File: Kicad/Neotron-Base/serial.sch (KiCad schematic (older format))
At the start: 7 parts, among them J601 Conn_02x05, U601 ICL3232CPZMAX

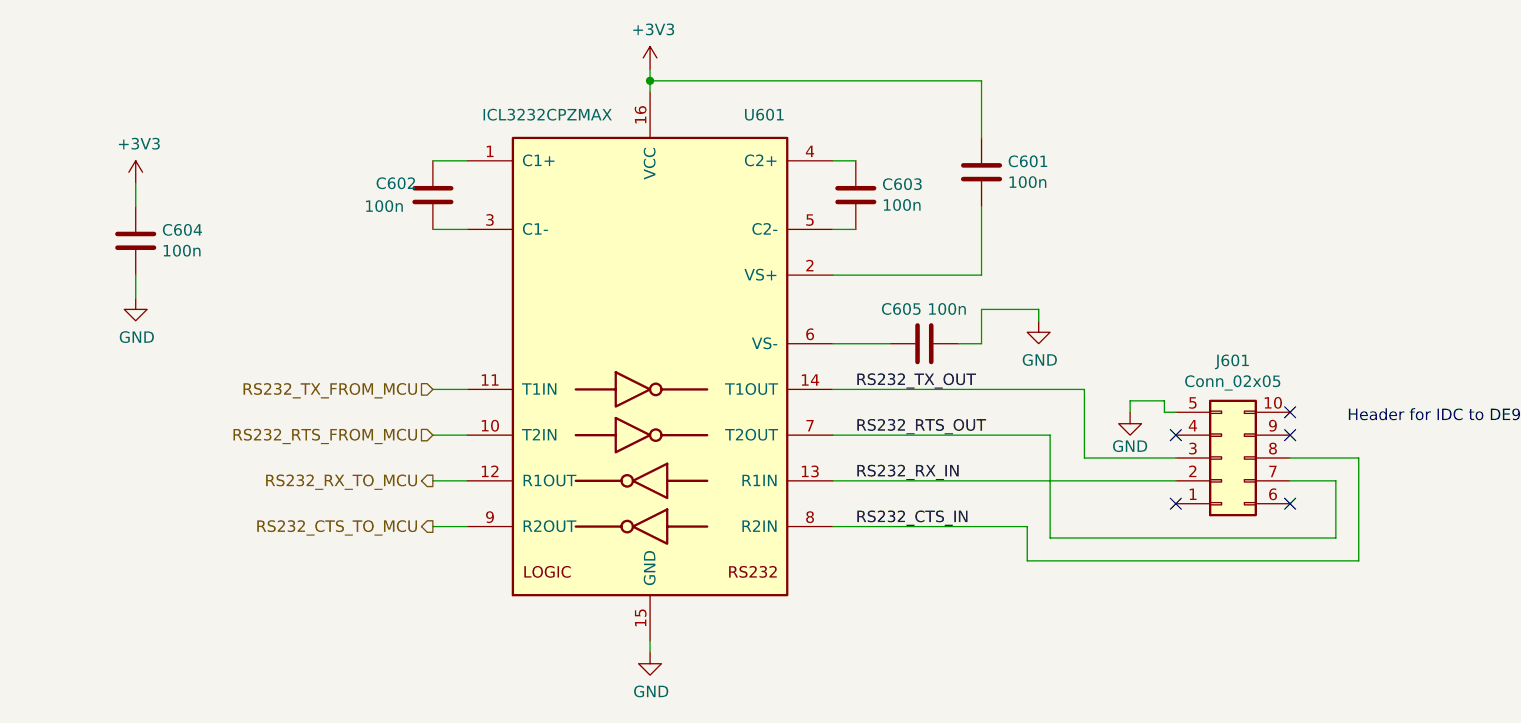
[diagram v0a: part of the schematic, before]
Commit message: Re-work CPU interface to include RMII.
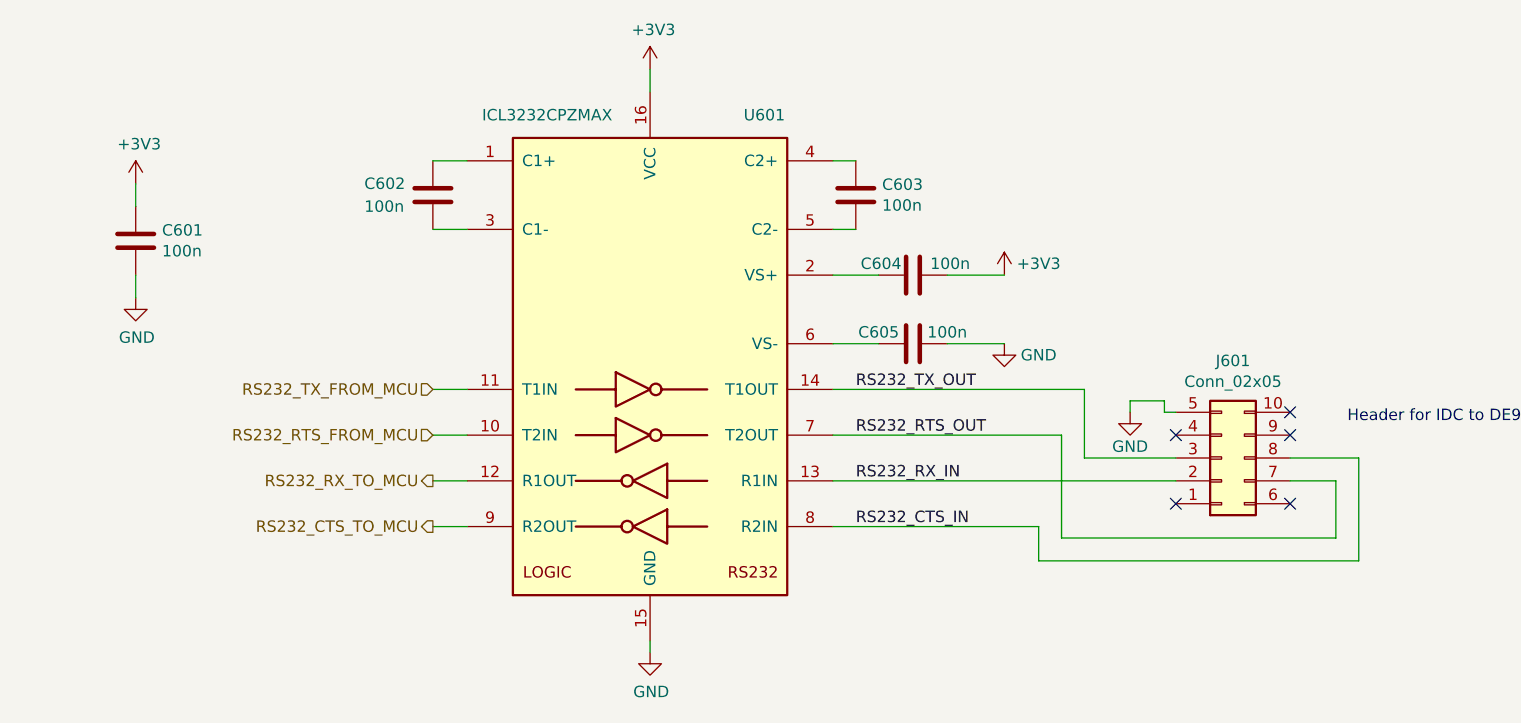
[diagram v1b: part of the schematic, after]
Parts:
- renumbered C604 to C601, C601 to C604
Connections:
- net +3V3: now also C604.2; no longer C604.1
- net at U601.2 (VS+): now also C604.1; no longer C604.2
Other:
- moved on the sheet: C604, C605
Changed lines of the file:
@@
 $Descr A4 11693 8268
 encoding utf-8
-Sheet 6 7
+Sheet 6 10
 Title "Neotron Base - RS-232 Interface"
-Date "2020-08-07"
+Date "2020-08-15"
 Rev "[Uncontrolled]"
 Comp "github.com/neotron-compute"
@@
 L power:GND #PWR?
 U 1 1 5E180507
-P 7300 3450
-F 0 "#PWR?" H 7300 3200 50  0001 C CNN
-F 1 "GND" H 7305 3277 50  0000 C CNN
-F 2 "" H 7300 3450 50  0001 C CNN
-F 3 "" H 7300 3450 50  0001 C CNN
-	1    7300 3450
-	1    0    0    -1
-$EndComp
-Wire Wire Line
-	7300 3450 7300 3400
+P 7150 3550
+F 0 "#PWR?" H 7150 3300 50  0001 C CNN
+F 1 "GND" H 7300 3500 50  0000 C CNN
+F 2 "" H 7150 3550 50  0001 C CNN
+F 3 "" H 7150 3550 50  0001 C CNN
+	1    7150 3550
+	1    0    0    -1
+$EndComp
 $Comp
 L Device:C C603
@@
 L Device:C C605
 U 1 1 5E182C3F
-P 6800 3550
-F 0 "C605" V 6650 3450 50  0000 C CNN
-F 1 "100n" V 6650 3650 50  0000 C CNN
-F 2 "Capacitor_THT:C_Disc_D3.0mm_W2.0mm_P2.50mm" H 6838 3400 50  0001 C CNN
-F 3 "~" H 6800 3550 50  0001 C CNN
-F 4 "Vishay" H 0   0   50  0001 C CNN "Manufacturer"
-F 5 "K474Z20Y5VE5TL2" H 0   0   50  0001 C CNN "mpn"
-F 6 "0" H 6800 3550 50  0001 C CNN "DNP"
-	1    6800 3550
+P 6750 3550
+F 0 "C605" V 6700 3400 50  0000 C CNN
+F 1 "100n" V 6700 3700 50  0000 C CNN
+F 2 "Capacitor_THT:C_Disc_D3.0mm_W2.0mm_P2.50mm" H 6788 3400 50  0001 C CNN
+F 3 "~" H 6750 3550 50  0001 C CNN
+F 4 "Vishay" H -50 0   50  0001 C CNN "Manufacturer"
+F 5 "K474Z20Y5VE5TL2" H -50 0   50  0001 C CNN "mpn"
+F 6 "0" H 6750 3550 50  0001 C CNN "DNP"
+	1    6750 3550
 	0    1    1    0
 $EndComp
@@
 U 1 1 5E182DBA
 P 4650 2900
-F 0 "C602" H 4900 2850 50  0000 R CNN
+F 0 "C602" H 4950 2850 50  0000 R CNN
 F 1 "100n" H 4950 2950 50  0000 R CNN
 F 2 "Capacitor_THT:C_Disc_D3.0mm_W2.0mm_P2.50mm" H 4688 2750 50  0001 C CNN
@@
 $EndComp
 $Comp
-L Device:C C604
+L Device:C C601
 U 1 1 5E183108
 P 3350 3100
-F 0 "C604" H 3235 3054 50  0000 R CNN
+F 0 "C601" H 3235 3054 50  0000 R CNN
 F 1 "100n" H 3235 3145 50  0000 R CNN
 F 2 "Capacitor_THT:C_Disc_D3.0mm_W2.0mm_P2.50mm" H 3388 2950 50  0001 C CNN
@@
 	1    0    0    -1
 $EndComp
-Wire Wire Line
-	5600 2350 5600 2400
 $Comp
 L power:+3V3 #PWR?
@@
 $EndComp
 Wire Wire Line
-	6400 3550 6650 3550
-Wire Wire Line
-	6950 3550 7050 3550
-Wire Wire Line
-	7050 3550 7050 3400
-Wire Wire Line
-	7050 3400 7300 3400
-Wire Wire Line
-	5600 2400 7050 2400
-Connection ~ 5600 2400
-Wire Wire Line
-	5600 2400 5600 2450
-Wire Wire Line
 	6400 2750 6500 2750
 Wire Wire Line
@@
 	4650 3050 4800 3050
 $Comp
-L Device:C C601
+L Device:C C604
 U 1 1 5E188858
-P 7050 2800
-F 0 "C601" H 7165 2846 50  0000 L CNN
-F 1 "100n" H 7165 2755 50  0000 L CNN
-F 2 "Capacitor_THT:C_Disc_D3.0mm_W2.0mm_P2.50mm" H 7088 2650 50  0001 C CNN
-F 3 "~" H 7050 2800 50  0001 C CNN
-F 4 "Vishay" H 0   0   50  0001 C CNN "Manufacturer"
-F 5 "K474Z20Y5VE5TL2" H 0   0   50  0001 C CNN "mpn"
-F 6 "0" H 7050 2800 50  0001 C CNN "DNP"
-	1    7050 2800
-	1    0    0    -1
-$EndComp
-Wire Wire Line
-	7050 2400 7050 2650
-Wire Wire Line
-	7050 2950 7050 3250
-Wire Wire Line
-	6400 3250 7050 3250
+P 6750 3250
+F 0 "C604" V 6800 3300 50  0000 L CNN
+F 1 "100n" V 6800 3000 50  0000 L CNN
+F 2 "Capacitor_THT:C_Disc_D3.0mm_W2.0mm_P2.50mm" H 6788 3100 50  0001 C CNN
+F 3 "~" H 6750 3250 50  0001 C CNN
+F 4 "Vishay" H -300 450 50  0001 C CNN "Manufacturer"
+F 5 "K474Z20Y5VE5TL2" H -300 450 50  0001 C CNN "mpn"
+F 6 "0" H 6750 3250 50  0001 C CNN "DNP"
+	1    6750 3250
+	0    -1   -1   0
+$EndComp
 $Comp
 L power:GND #PWR?
@@
 	7500 3750 6400 3750
 Wire Wire Line
-	6400 4150 7900 4150
-Wire Wire Line
 	7900 4050 7500 4050
 Wire Wire Line
 	7500 3750 7500 4050
 Wire Wire Line
-	6400 3950 7350 3950
+	6400 3950 7400 3950
 Wire Wire Line
 	8700 4050 8400 4050
@@
 	8600 4150 8400 4150
 Wire Wire Line
-	7250 4350 7250 4500
-Wire Wire Line
-	6400 4350 7250 4350
+	7300 4350 7300 4500
+Wire Wire Line
+	6400 4350 7300 4350
 Wire Wire Line
 	8600 4150 8600 4400
 Wire Wire Line
-	7350 3950 7350 4400
-Wire Wire Line
-	7350 4400 8600 4400
-Wire Wire Line
-	7250 4500 8700 4500
+	7400 3950 7400 4400
+Wire Wire Line
+	7400 4400 8600 4400
 Wire Wire Line
 	8700 4050 8700 4500
@@
 Text Notes 550  7700 0    50   Italic 0
 This chip is a 3.3V capable version of the MAX232 RS-232 level shifter. The port is wired DTE (i.e. as if this was an IBM PC, rather than\nas a modem). We only have a five-wire RS-232 interface, missing the Ring Input, Data Set Ready, Data Terminal Ready and Carrier Detect\npins.\n\nIf you want a proper DE9 RS-232 port, you will need a 10-way IDC ribbon to DE9 male cable. These were commonly fitted to PCs in the 1990s\nas the ISA I/O expansion cards and/or motherboards of the time often didn't have room for all of the ports on the backplate. We didn't\nfit a DE9 to this board due to similar space issues.
+Wire Wire Line
+	6400 3550 6600 3550
+Wire Wire Line
+	6400 3250 6600 3250
+Wire Wire Line
+	5600 2350 5600 2450
+$Comp
+L power:+3V3 #PWR?
+U 1 1 5F40D603
+P 7150 3250
+F 0 "#PWR?" H 7150 3100 50  0001 C CNN
+F 1 "+3V3" H 7300 3300 50  0000 C CNN
+F 2 "" H 7150 3250 50  0001 C CNN
+F 3 "" H 7150 3250 50  0001 C CNN
+	1    7150 3250
+	1    0    0    -1
+$EndComp
+Wire Wire Line
+	6900 3550 7150 3550
+Wire Wire Line
+	6900 3250 7150 3250
+Wire Wire Line
+	6400 4150 7900 4150
+Wire Wire Line
+	7300 4500 8700 4500
 $EndSCHEMATC
